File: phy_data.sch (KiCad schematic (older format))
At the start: 16 parts, among them J6 RJ45_LED_Shielded, J7 RJ45_LED_Shielded, J8 RJ45_LED_Shielded, J9 RJ45_LED_Shielded, U4 88E1545

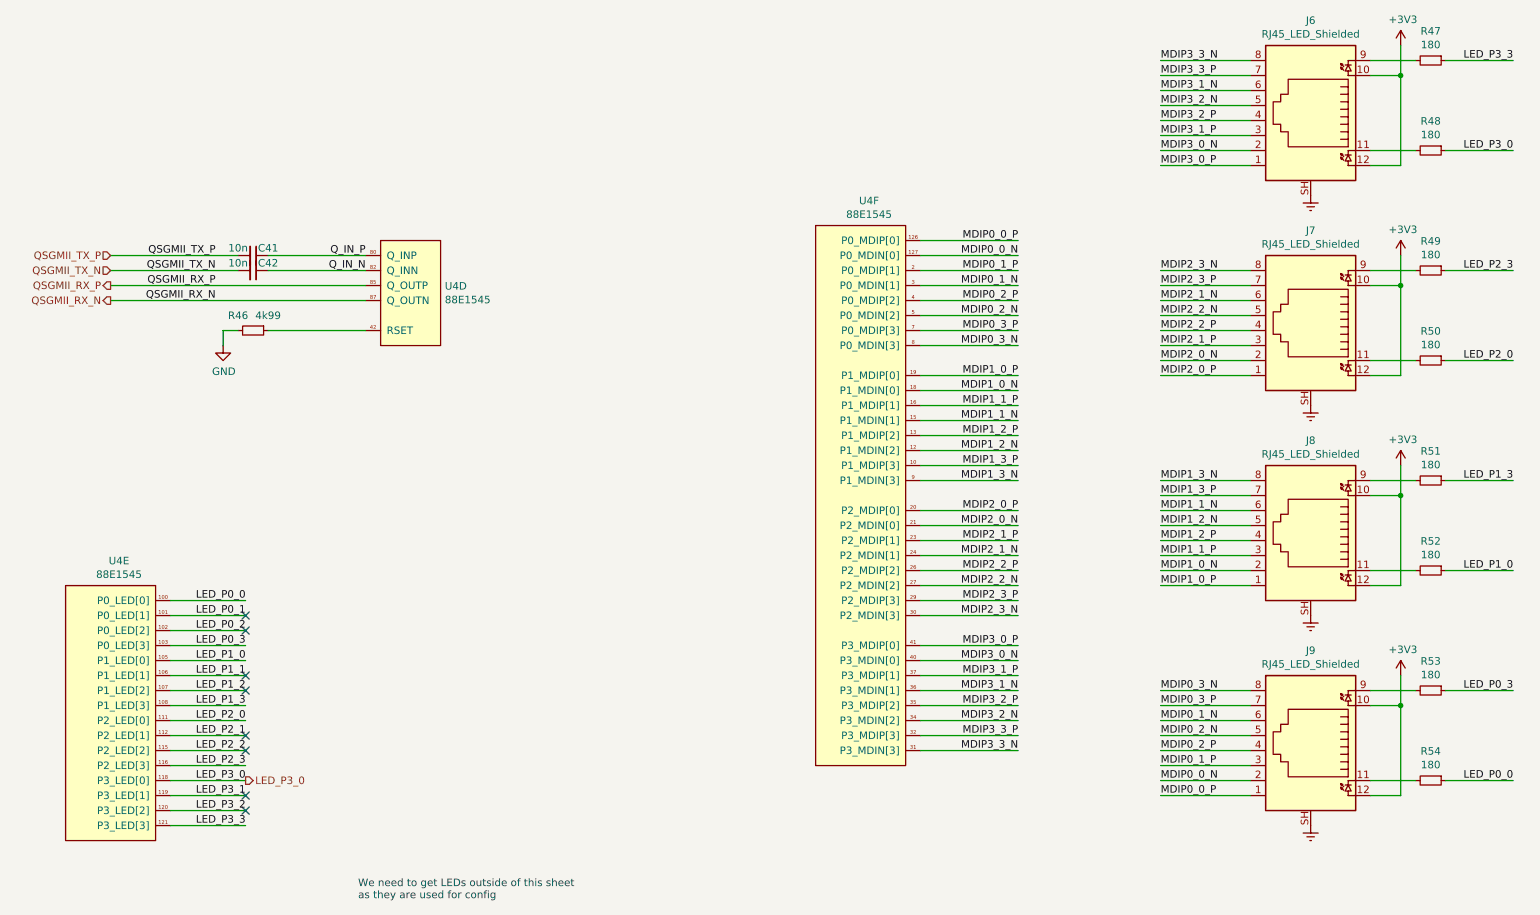
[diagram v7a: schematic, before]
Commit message: sch: Swap individual RJ45 with RJSAE connector
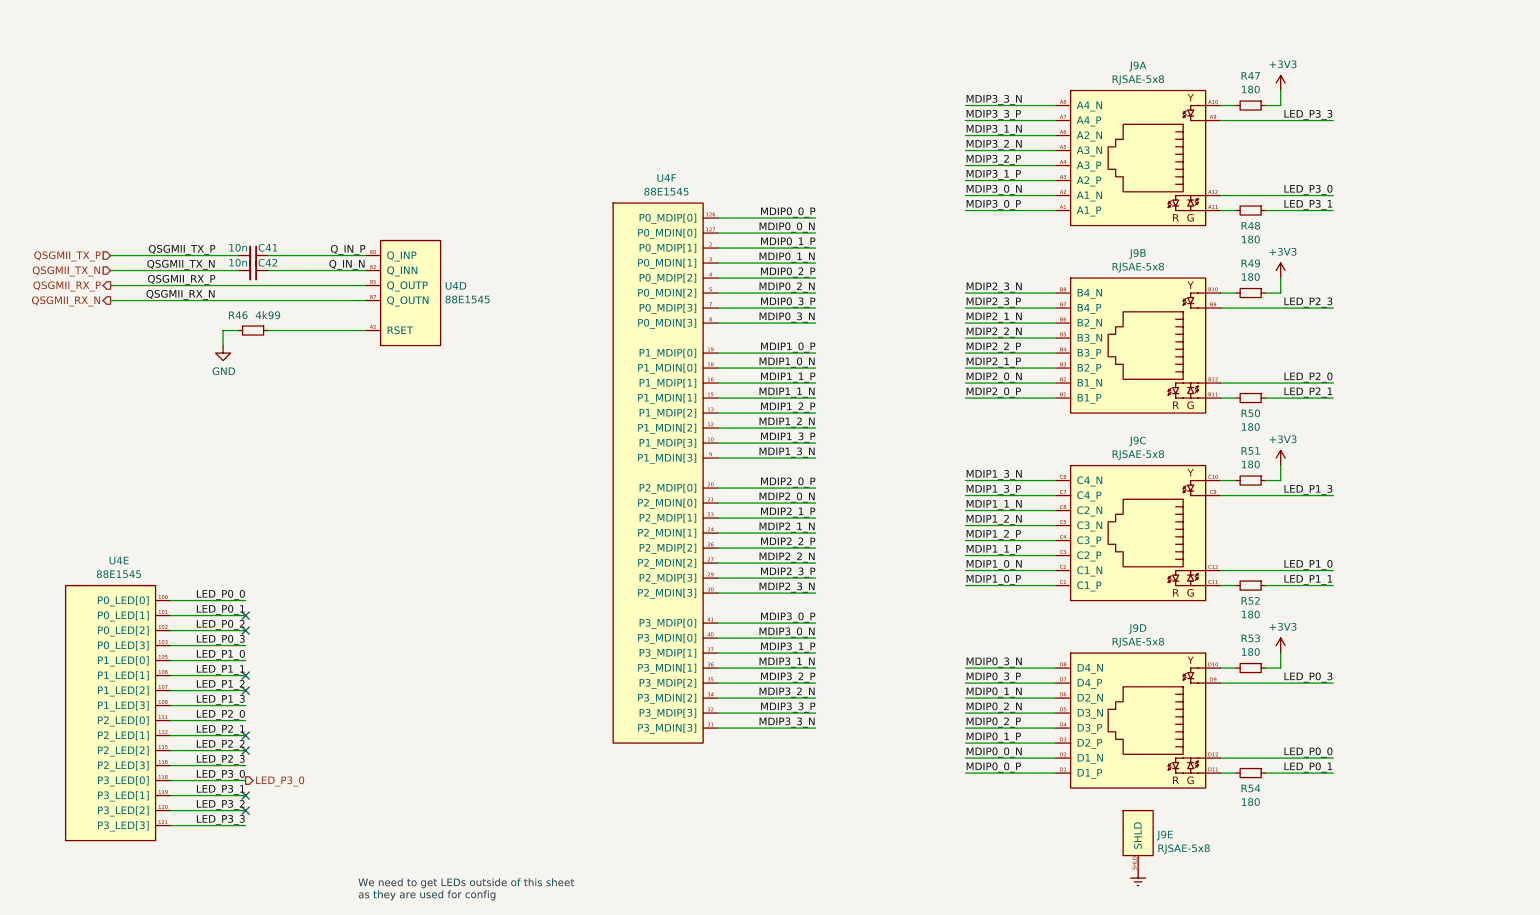
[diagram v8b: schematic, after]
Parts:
- removed J6, J7, J8, J9: RJ45_LED_Shielded, Connector_RJ:RJ45_Amphenol_RJHSE538X, symbol Connector:RJ45_LED_Shielded
- added J9: RJSAE-5x8, pimouss-motherboard:RJSAE-5x8, symbol pimouss-motherboard:RJSAE-5x8
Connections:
- net +3V3: now also R47.1, R49.1, R51.1, R53.1
- net Earth: now also J9.SHLD
- net LED_P0_0: now also J9.D12; no longer R54.1
- net LED_P0_1: now also R54.1
- net LED_P0_3: now also J9.D9; no longer R53.1
- net LED_P1_0: now also J9.C12; no longer R52.1
- net LED_P1_1: now also R52.1
- net LED_P1_3: now also J9.C9; no longer R51.1
- net LED_P2_0: now also J9.B12; no longer R50.1
- net LED_P2_1: now also R50.1
- net LED_P2_3: now also J9.B9; no longer R49.1
- net LED_P3_0: now also J9.A12; no longer R48.1
- net LED_P3_1: now also R48.1
- net LED_P3_3: now also J9.A9; no longer R47.1
- net MDIP0_0_N: now also J9.D2 (D1_N)
- net MDIP0_0_P: now also J9.D1 (D1_P)
- net MDIP0_1_N: now also J9.D6 (D2_N)
- net MDIP0_1_P: now also J9.D3 (D2_P)
- net MDIP0_2_N: now also J9.D5 (D3_N)
- net MDIP0_2_P: now also J9.D4 (D3_P)
- net MDIP0_3_N: now also J9.D8 (D4_N)
- net MDIP0_3_P: now also J9.D7 (D4_P)
- net MDIP1_0_N: now also J9.C2 (C1_N)
- net MDIP1_0_P: now also J9.C1 (C1_P)
- net MDIP1_1_N: now also J9.C6 (C2_N)
- net MDIP1_1_P: now also J9.C3 (C2_P)
- net MDIP1_2_N: now also J9.C5 (C3_N)
- net MDIP1_2_P: now also J9.C4 (C3_P)
- net MDIP1_3_N: now also J9.C8 (C4_N)
- net MDIP1_3_P: now also J9.C7 (C4_P)
- net MDIP2_0_N: now also J9.B2 (B1_N)
- net MDIP2_0_P: now also J9.B1 (B1_P)
- net MDIP2_1_N: now also J9.B6 (B2_N)
- net MDIP2_1_P: now also J9.B3 (B2_P)
- net MDIP2_2_N: now also J9.B5 (B3_N)
- net MDIP2_2_P: now also J9.B4 (B3_P)
- net MDIP2_3_N: now also J9.B8 (B4_N)
- net MDIP2_3_P: now also J9.B7 (B4_P)
- net MDIP3_0_N: now also J9.A2 (A1_N)
- net MDIP3_0_P: now also J9.A1 (A1_P)
- net MDIP3_1_N: now also J9.A6 (A2_N)
- net MDIP3_1_P: now also J9.A3 (A2_P)
- net MDIP3_2_N: now also J9.A5 (A3_N)
- net MDIP3_2_P: now also J9.A4 (A3_P)
- net MDIP3_3_N: now also J9.A8 (A4_N)
- net MDIP3_3_P: now also J9.A7 (A4_P)
- net at R48.2: now also J9.A11
- net at R47.2: now also J9.A10
- net at R50.2: now also J9.B11
- net at R49.2: now also J9.B10
- net at R52.2: now also J9.C11
- net at R51.2: now also J9.C10
- net at R54.2: now also J9.D11
- net at R53.2: now also J9.D10
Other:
- moved on the sheet: R47, R48, R49, R50, R51, R52, R53, R54, U4F
